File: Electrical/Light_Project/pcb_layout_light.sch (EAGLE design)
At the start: 9 parts, among them U1 REG710NA-3.3/3K, U2 ATTINY85V-10SU, U3 FSM8JRT

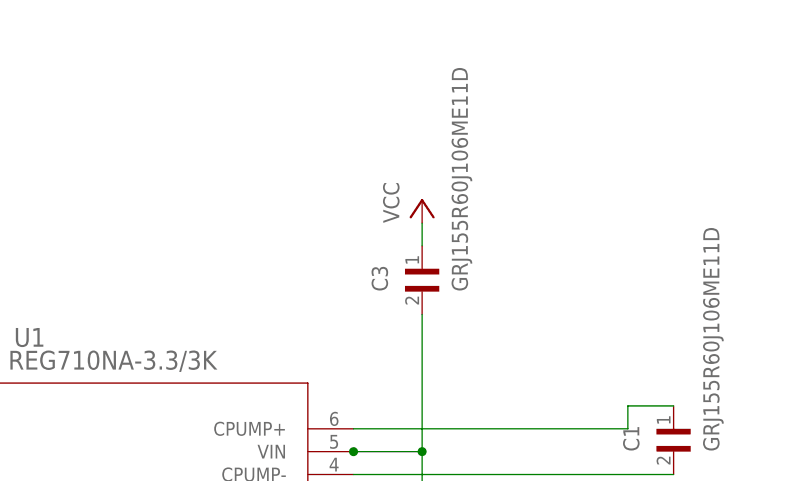
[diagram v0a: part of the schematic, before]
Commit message: add updated solidwords files with screws and nuts
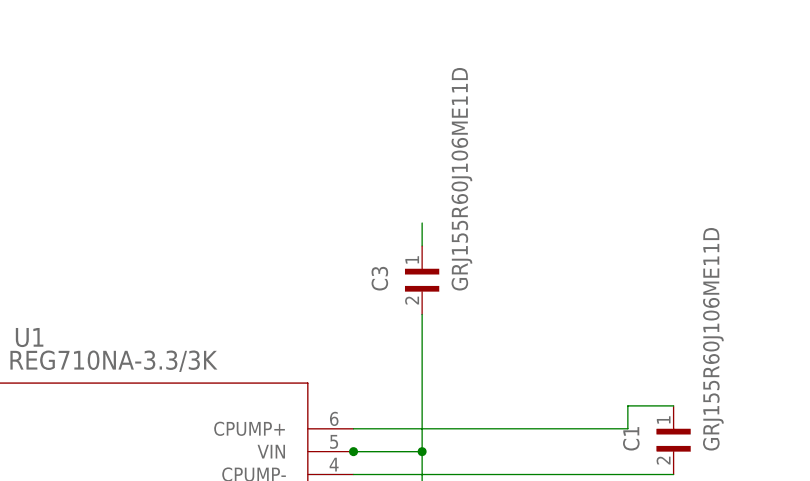
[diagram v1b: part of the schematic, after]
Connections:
- net VCC renamed N$8
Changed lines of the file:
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@@
 <part name="U2" library="attiny85" deviceset="ATTINY85V-10SU" device=""/>
 <part name="GND1" library="supply1" library_urn="urn:adsk.eagle:library:371" deviceset="GND" device=""/>
-<part name="P+1" library="supply1" library_urn="urn:adsk.eagle:library:371" deviceset="VCC" device=""/>
 <part name="GND2" library="supply1" library_urn="urn:adsk.eagle:library:371" deviceset="GND" device=""/>
 <part name="GND3" library="supply1" library_urn="urn:adsk.eagle:library:371" deviceset="GND" device=""/>
@@
 <instance part="GND1" gate="1" x="-15.24" y="83.82" smashed="yes" rot="R270">
 <attribute name="VALUE" x="-17.78" y="86.36" size="1.778" layer="96" rot="R270"/>
-</instance>
-<instance part="P+1" gate="VCC" x="86.36" y="111.76" smashed="yes">
-<attribute name="VALUE" x="83.82" y="109.22" size="1.778" layer="96" rot="R90"/>
 </instance>
 <instance part="GND2" gate="1" x="2.54" y="-20.32" smashed="yes">
@@
 </segment>
 </net>
-<net name="VCC" class="0">
-<segment>
-<pinref part="P+1" gate="VCC" pin="VCC"/>
-<pinref part="C3" gate="G$1" pin="1"/>
-<wire x1="86.36" y1="109.22" x2="86.36" y2="106.68" width="0.1524" layer="91"/>
-</segment>
-</net>
 <net name="N$6" class="0">
 <segment>
@@
 </segment>
 </net>
+<net name="N$8" class="0">
+<segment>
+<pinref part="C3" gate="G$1" pin="1"/>
+<wire x1="86.36" y1="109.22" x2="86.36" y2="106.68" width="0.1524" layer="91"/>
+</segment>
+</net>

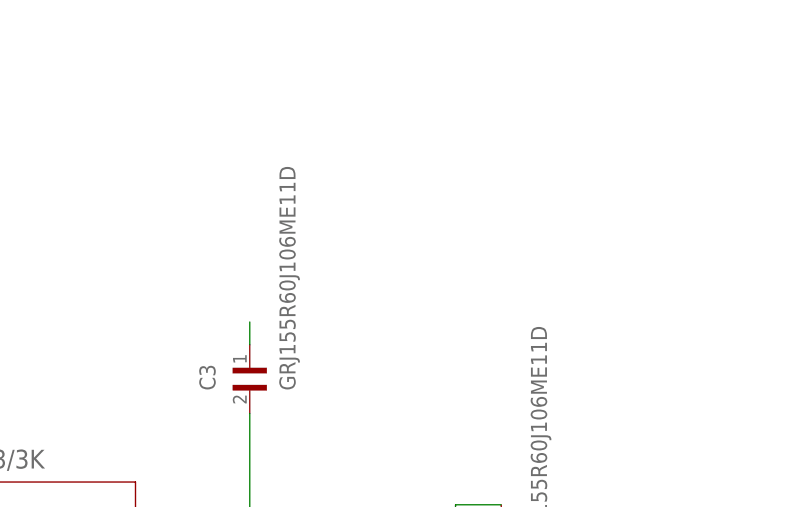
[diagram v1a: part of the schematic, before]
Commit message: Update bypass cap to go to ground and add header pins for switch and power supply
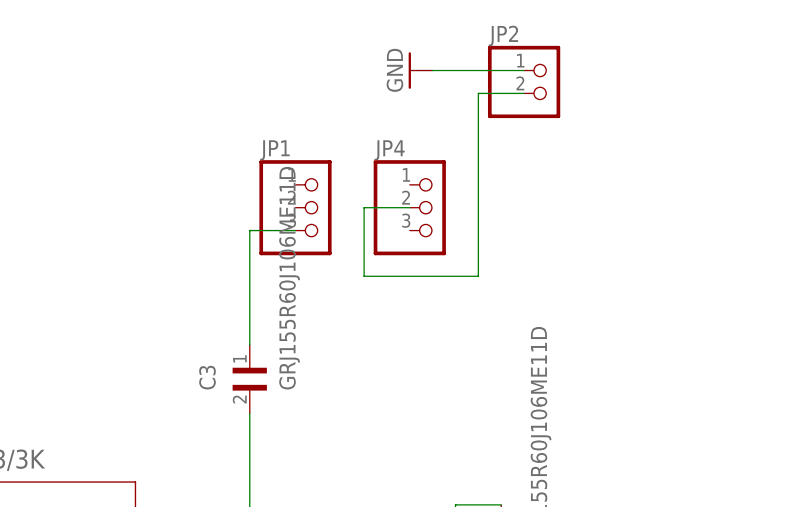
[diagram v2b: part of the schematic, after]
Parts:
- added JP1, JP4: (no value), pinhead:PINHD-1X3
- added JP2: (no value), pinhead:PINHD-1X2
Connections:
- new net N$10: JP2.2, JP4.2
- net GND: now also JP2.1
- net N$8: now also JP1.3
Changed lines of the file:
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@@
 <part name="GND4" library="supply1" library_urn="urn:adsk.eagle:library:371" deviceset="GND" device=""/>
 <part name="R2" library="1p1koSF" deviceset="RR0816P-112-D" device=""/>
+<part name="JP2" library="pinhead" library_urn="urn:adsk.eagle:library:325" deviceset="PINHD-1X2" device="" package3d_urn="urn:adsk.eagle:package:22435/2"/>
+<part name="GND5" library="supply1" library_urn="urn:adsk.eagle:library:371" deviceset="GND" device=""/>
+<part name="JP1" library="pinhead" library_urn="urn:adsk.eagle:library:325" deviceset="PINHD-1X3" device="" package3d_urn="urn:adsk.eagle:package:22458/2"/>
+<part name="JP4" library="pinhead" library_urn="urn:adsk.eagle:library:325" deviceset="PINHD-1X3" device="" package3d_urn="urn:adsk.eagle:package:22458/2"/>
 </parts>
 <sheets>
@@
 <attribute name="NAME" x="195.9356" y="-25.8572" size="3.4798" layer="95" ratio="10" rot="SR0"/>
 </instance>
+<instance part="JP2" gate="G$1" x="119.38" y="134.62" smashed="yes">
+<attribute name="NAME" x="113.03" y="140.335" size="1.778" layer="95"/>
+<attribute name="VALUE" x="113.03" y="129.54" size="1.778" layer="96"/>
+</instance>
+<instance part="GND5" gate="1" x="104.14" y="137.16" smashed="yes" rot="R270">
+<attribute name="VALUE" x="101.6" y="139.7" size="1.778" layer="96" rot="R270"/>
+</instance>
+<instance part="JP1" gate="A" x="93.98" y="121.92" smashed="yes">
+<attribute name="NAME" x="87.63" y="127.635" size="1.778" layer="95"/>
+<attribute name="VALUE" x="87.63" y="114.3" size="1.778" layer="96"/>
+</instance>
+<instance part="JP4" gate="A" x="106.68" y="121.92" smashed="yes">
+<attribute name="NAME" x="100.33" y="127.635" size="1.778" layer="95"/>
+<attribute name="VALUE" x="100.33" y="114.3" size="1.778" layer="96"/>
+</instance>
 </instances>
 <busses>
@@
 <pinref part="D1" gate="G$1" pin="C"/>
 <pinref part="GND4" gate="1" pin="GND"/>
+</segment>
+<segment>
+<pinref part="JP2" gate="G$1" pin="1"/>
+<wire x1="116.84" y1="137.16" x2="106.68" y2="137.16" width="0.1524" layer="91"/>
+<pinref part="GND5" gate="1" pin="GND"/>
 </segment>
 </net>
@@
 <segment>
 <pinref part="C3" gate="G$1" pin="1"/>
-<wire x1="86.36" y1="109.22" x2="86.36" y2="106.68" width="0.1524" layer="91"/>
-</segment>
-</net>
+<wire x1="86.36" y1="119.38" x2="86.36" y2="106.68" width="0.1524" layer="91"/>
+<pinref part="JP1" gate="A" pin="3"/>
+<wire x1="86.36" y1="119.38" x2="91.44" y2="119.38" width="0.1524" layer="91"/>
+</segment>
+</net>
+<net name="N$10" class="0">
+<segment>
+<wire x1="111.76" y1="114.3" x2="111.76" y2="134.62" width="0.1524" layer="91"/>
+<pinref part="JP2" gate="G$1" pin="2"/>
+<wire x1="116.84" y1="134.62" x2="111.76" y2="134.62" width="0.1524" layer="91"/>
+<pinref part="JP4" gate="A" pin="2"/>
+<wire x1="104.14" y1="121.92" x2="99.06" y2="121.92" width="0.1524" layer="91"/>
+<wire x1="99.06" y1="121.92" x2="99.06" y2="114.3" width="0.1524" layer="91"/>
+<wire x1="99.06" y1="114.3" x2="111.76" y2="114.3" width="0.1524" layer="91"/>
+</segment>
+</net>

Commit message: Add BOM
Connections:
- removed net N$4: C3.2, U1.ENABLE, U1.VIN
- net GND: now also C3.2
- net N$8: now also U1.ENABLE, U1.VIN
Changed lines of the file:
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@@
 <part name="JP1" library="pinhead" library_urn="urn:adsk.eagle:library:325" deviceset="PINHD-1X3" device="" package3d_urn="urn:adsk.eagle:package:22458/2"/>
 <part name="JP4" library="pinhead" library_urn="urn:adsk.eagle:library:325" deviceset="PINHD-1X3" device="" package3d_urn="urn:adsk.eagle:package:22458/2"/>
+<part name="GND6" library="supply1" library_urn="urn:adsk.eagle:library:371" deviceset="GND" device=""/>
 </parts>
 <sheets>
@@
 <attribute name="VALUE" x="100.33" y="114.3" size="1.778" layer="96"/>
 </instance>
+<instance part="GND6" gate="1" x="73.66" y="99.06" smashed="yes" rot="R270">
+<attribute name="VALUE" x="71.12" y="101.6" size="1.778" layer="96" rot="R270"/>
+</instance>
 </instances>
 <busses>
@@
 <wire x1="116.84" y1="137.16" x2="106.68" y2="137.16" width="0.1524" layer="91"/>
 <pinref part="GND5" gate="1" pin="GND"/>
+</segment>
+<segment>
+<wire x1="86.36" y1="99.06" x2="76.2" y2="99.06" width="0.1524" layer="91"/>
+<pinref part="GND6" gate="1" pin="GND"/>
+<pinref part="C3" gate="G$1" pin="2"/>
 </segment>
 </net>
@@
 </segment>
 </net>
-<net name="N$4" class="0">
-<segment>
-<pinref part="U1" gate="A" pin="VIN"/>
-<wire x1="78.74" y1="83.82" x2="86.36" y2="83.82" width="0.1524" layer="91"/>
-<junction x="78.74" y="83.82"/>
-<pinref part="U1" gate="A" pin="ENABLE"/>
-<wire x1="12.7" y1="81.28" x2="12.7" y2="71.12" width="0.1524" layer="91"/>
-<wire x1="12.7" y1="71.12" x2="86.36" y2="71.12" width="0.1524" layer="91"/>
-<wire x1="86.36" y1="71.12" x2="86.36" y2="83.82" width="0.1524" layer="91"/>
-<pinref part="C3" gate="G$1" pin="2"/>
-<wire x1="86.36" y1="99.06" x2="86.36" y2="83.82" width="0.1524" layer="91"/>
-<junction x="86.36" y="83.82"/>
-</segment>
-</net>
 <net name="N$5" class="0">
 <segment>
@@
 </segment>
 </net>
-<net name="N$8" class="0">
-<segment>
-<pinref part="C3" gate="G$1" pin="1"/>
-<wire x1="86.36" y1="119.38" x2="86.36" y2="106.68" width="0.1524" layer="91"/>
-<pinref part="JP1" gate="A" pin="3"/>
-<wire x1="86.36" y1="119.38" x2="91.44" y2="119.38" width="0.1524" layer="91"/>
-</segment>
-</net>
 <net name="N$10" class="0">
 <segment>
@@
 </segment>
 </net>
+<net name="N$8" class="0">
+<segment>
+<pinref part="C3" gate="G$1" pin="1"/>
+<wire x1="86.36" y1="106.68" x2="86.36" y2="109.22" width="0.1524" layer="91"/>
+<pinref part="JP1" gate="A" pin="3"/>
+<wire x1="86.36" y1="109.22" x2="86.36" y2="119.38" width="0.1524" layer="91"/>
+<wire x1="86.36" y1="119.38" x2="91.44" y2="119.38" width="0.1524" layer="91"/>
+<wire x1="86.36" y1="109.22" x2="93.98" y2="109.22" width="0.1524" layer="91"/>
+<junction x="86.36" y="109.22"/>
+<wire x1="93.98" y1="109.22" x2="93.98" y2="96.52" width="0.1524" layer="91"/>
+<wire x1="93.98" y1="96.52" x2="86.36" y2="96.52" width="0.1524" layer="91"/>
+<pinref part="U1" gate="A" pin="VIN"/>
+<wire x1="78.74" y1="83.82" x2="86.36" y2="83.82" width="0.1524" layer="91"/>
+<junction x="78.74" y="83.82"/>
+<pinref part="U1" gate="A" pin="ENABLE"/>
+<wire x1="12.7" y1="81.28" x2="12.7" y2="71.12" width="0.1524" layer="91"/>
+<wire x1="12.7" y1="71.12" x2="86.36" y2="71.12" width="0.1524" layer="91"/>
+<wire x1="86.36" y1="71.12" x2="86.36" y2="83.82" width="0.1524" layer="91"/>
+<wire x1="86.36" y1="96.52" x2="86.36" y2="83.82" width="0.1524" layer="91"/>
+<junction x="86.36" y="83.82"/>
+</segment>
+</net>
